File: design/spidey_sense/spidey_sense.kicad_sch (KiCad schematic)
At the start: 10 parts, among them J1 Input_Screw_Terminal, J10 Output_Screw_Terminal, J2 Thermocouple_Terminal, J3 Thermocouple_Terminal, J4 Thermocouple_Terminal, J5 Thermocouple_Terminal, J6 Conn_01x06_Female, J7 Conn_01x06_Female, J8 Conn_01x06_Female, J9 Conn_01x06_Female

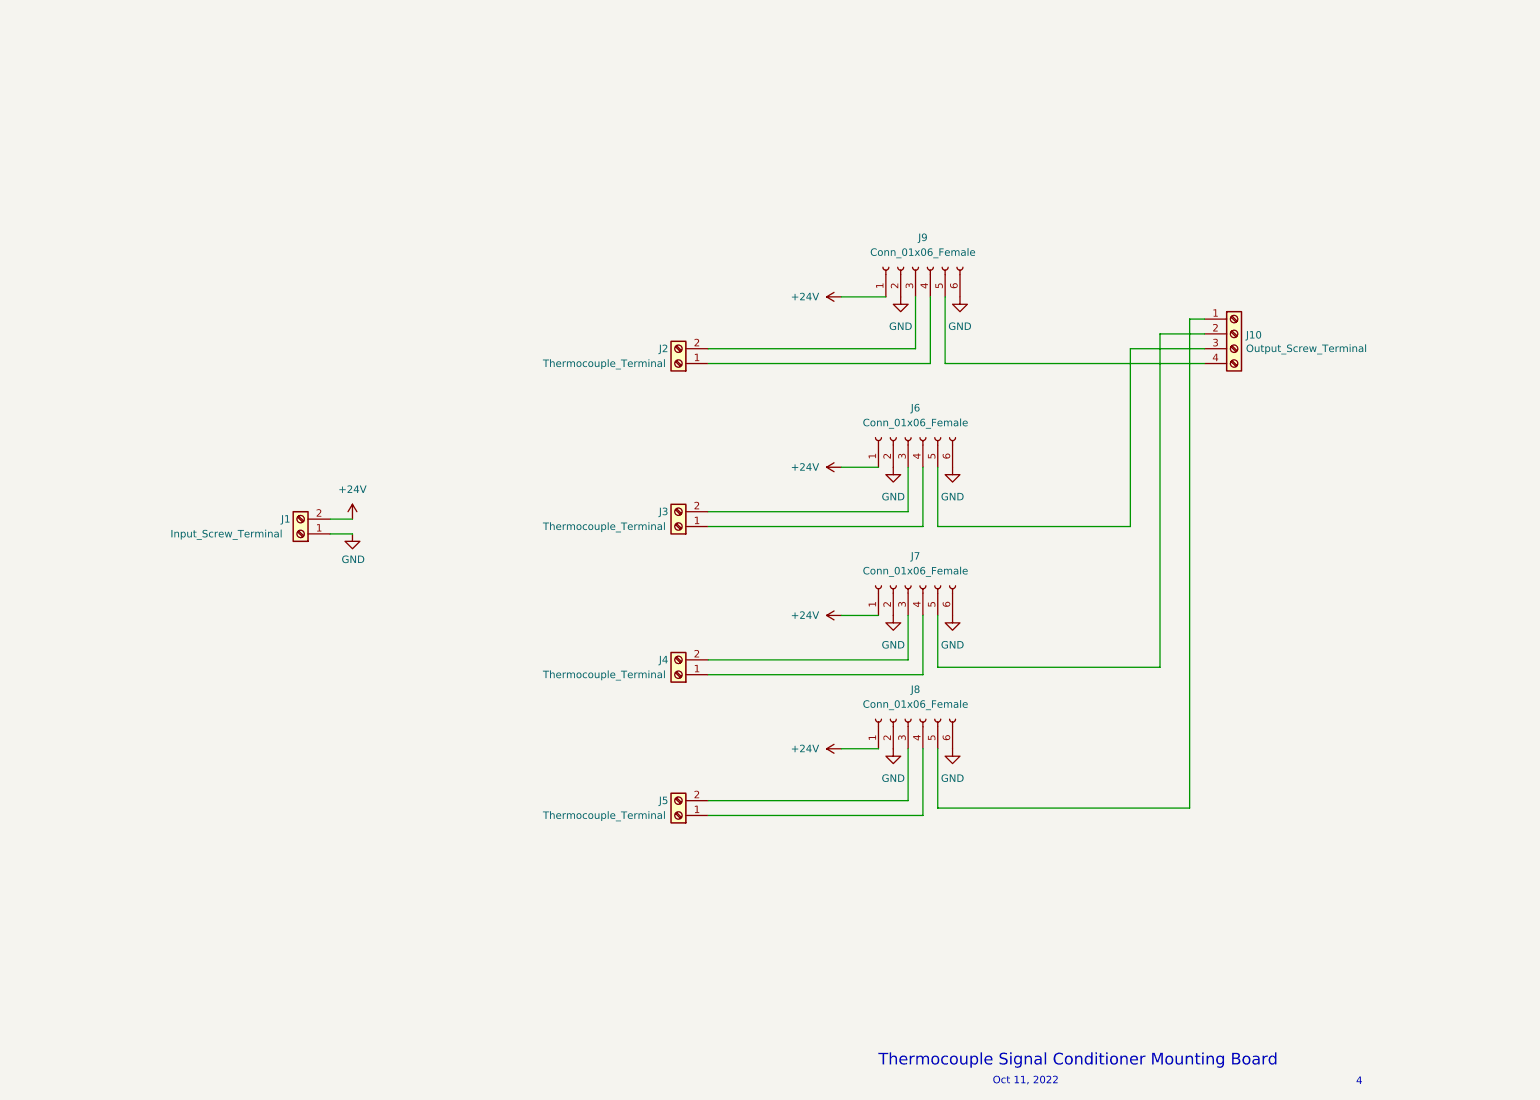
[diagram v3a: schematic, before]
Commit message: Changed component orientations and added labels
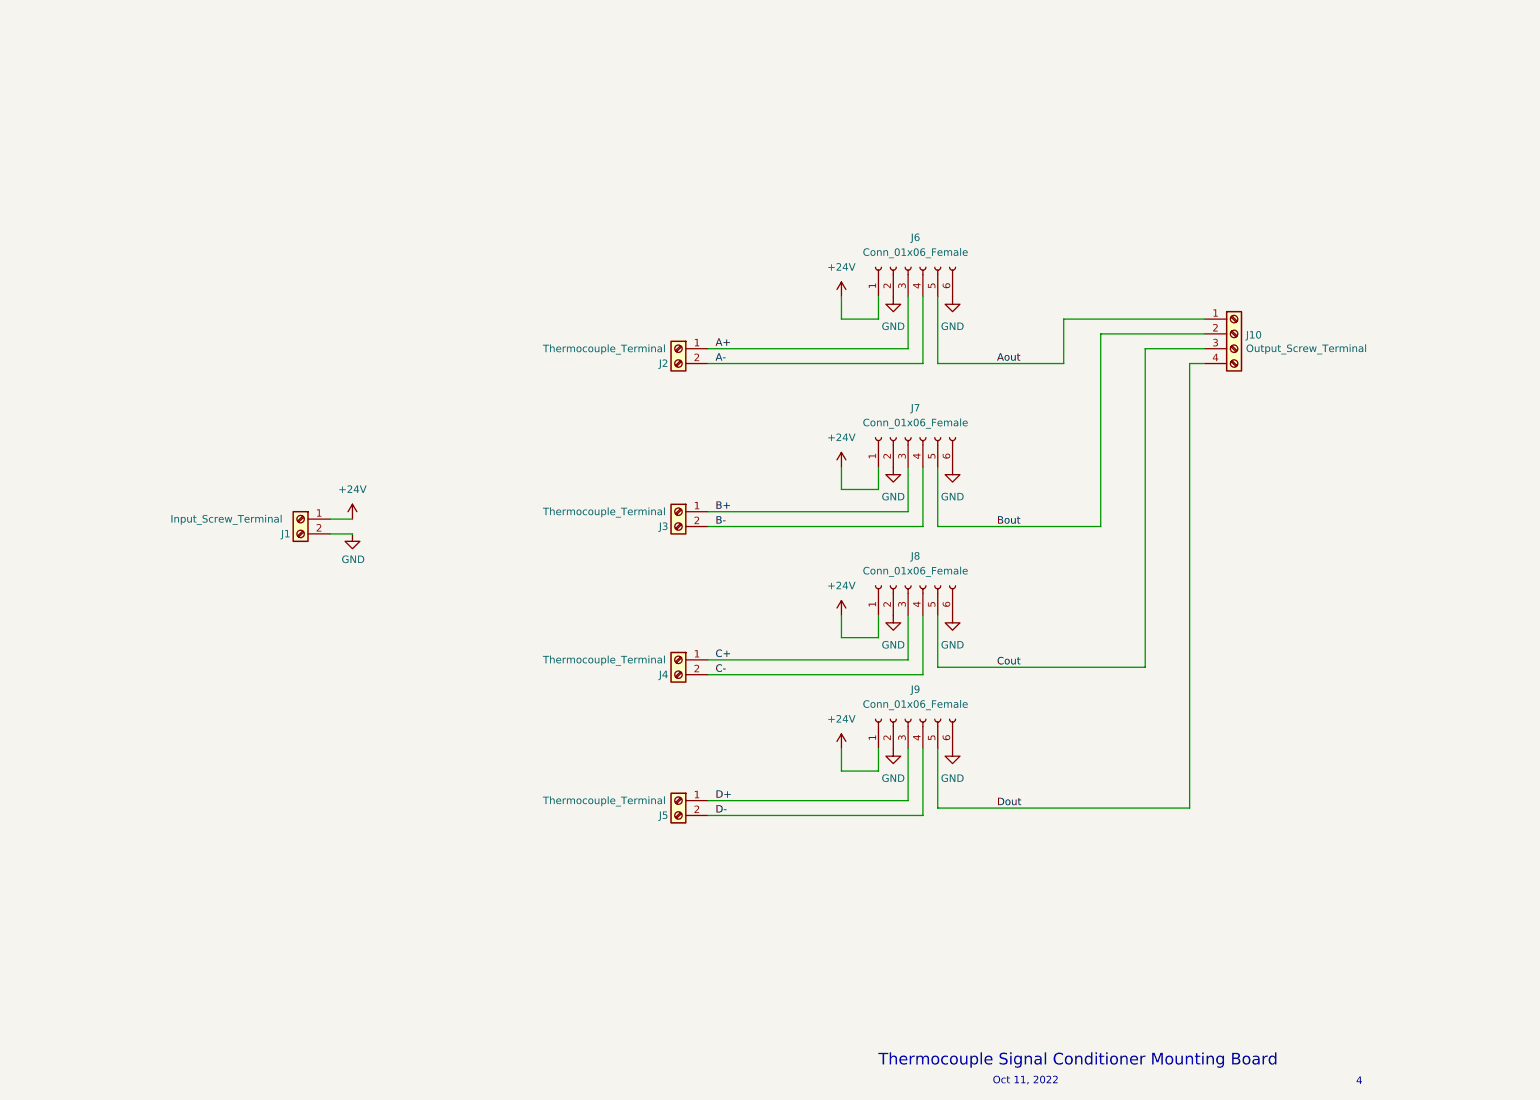
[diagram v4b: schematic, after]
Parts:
- renumbered J9 to J6, J6 to J7, J7 to J8, J8 to J9
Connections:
- net +24V: now also J1.1 (Pin_1); no longer J1.2 (Pin_2)
- net GND: now also J1.2 (Pin_2); no longer J1.1 (Pin_1)
- net Aout: now reaches J10.1 (Pin_1)
- net Aout: now also J6.5 (Pin_5); no longer J9.5 (Pin_5)
- net Bout: now reaches J10.2 (Pin_2)
- net Bout: now also J7.5 (Pin_5); no longer J8.5 (Pin_5)
- net Cout: now reaches J10.3 (Pin_3)
- net Cout: now also J8.5 (Pin_5); no longer J7.5 (Pin_5)
- net Dout: now reaches J10.4 (Pin_4)
- net Dout: now also J9.5 (Pin_5); no longer J6.5 (Pin_5)
- net A+: now reaches J2.1 (Pin_1)
- net A+: now also J6.3 (Pin_3); no longer J6.4 (Pin_4)
- net A-: now reaches J2.2 (Pin_2)
- net A-: now also J6.4 (Pin_4); no longer J6.3 (Pin_3)
- net B+: now reaches J3.1 (Pin_1)
- net B+: now also J7.3 (Pin_3); no longer J7.4 (Pin_4)
- net B-: now reaches J3.2 (Pin_2)
- net B-: now also J7.4 (Pin_4); no longer J7.3 (Pin_3)
- net C+: now reaches J4.1 (Pin_1)
- net C+: now also J8.3 (Pin_3); no longer J8.4 (Pin_4)
- net C-: now reaches J4.2 (Pin_2)
- net C-: now also J8.4 (Pin_4); no longer J8.3 (Pin_3)
- net D+: now reaches J5.1 (Pin_1)
- net D+: now also J9.3 (Pin_3); no longer J9.4 (Pin_4)
- net D-: now reaches J5.2 (Pin_2)
- net D-: now also J9.4 (Pin_4); no longer J9.3 (Pin_3)
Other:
- moved on the sheet: J1, J2, J3, J4, J5, J6
